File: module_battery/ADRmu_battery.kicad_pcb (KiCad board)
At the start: 2 copper layers, 160 x 100 mm, 1 part, among them J101 Harting 09042326831

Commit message: asdf
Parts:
- removed J101: Harting 09042326831, Connector_DIN:DIN41612_D_2x16_Male_Horizontal_THT
- added B101: BK-18650-PC8, ADRmu_battery_Library:BK-18650-PC8, F.Cu at (115.0, 70.0)
- added J1: Harting 09042326831, Connector_DIN:DIN41612_D_2x16_Male_Horizontal_THT, F.Cu at (224.7, 60.6)

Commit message: asdf
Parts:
- added C101: 1u 50V, Capacitor_SMD:C_0805_2012Metric, F.Cu at (148.6, 97.8)
- added C102: 1u 50V, Capacitor_SMD:C_0805_2012Metric, F.Cu at (144.1, 94.8)
- added C103: 1u 50V, Capacitor_SMD:C_0805_2012Metric, F.Cu at (144.1, 91.8)
- added C104: 1u 50V, Capacitor_SMD:C_0805_2012Metric, F.Cu at (139.8, 104.7)
- added C105: 1u 50V, Capacitor_SMD:C_0805_2012Metric, F.Cu at (153.0, 91.8)
- added C106: 1u 50V, Capacitor_SMD:C_0805_2012Metric, F.Cu at (148.6, 91.8)
- added C107: 1u 50V, Capacitor_SMD:C_0805_2012Metric, F.Cu at (135.4, 104.7)
- added C108: 100n 50V, Capacitor_SMD:C_0805_2012Metric, F.Cu at (144.1, 97.8)
- added C109: 100n 50V, Capacitor_SMD:C_0805_2012Metric, F.Cu at (148.6, 94.8)
- added C110: 100n 50V, Capacitor_SMD:C_0805_2012Metric, F.Cu at (142.9, 101.1)
- added C111: 100n 50V, Capacitor_SMD:C_0805_2012Metric, F.Cu at (168.9, 111.8)
- added D101: 1N4148, Diode_SMD:D_SOD-123, F.Cu at (169.6, 104.0)
- added D102: 16V, Diode_SMD:D_SOT-23_ANK, F.Cu at (168.9, 108.0)
- added NT101: NetTie_2, NetTie:NetTie-2_SMD_Pad2.0mm, F.Cu at (136.9, 101.4)
- added Q101: Q_NMOS_GDS, Package_TO_SOT_SMD:TO-252-2, F.Cu at (160.6, 114.4)
- added Q102: Q_NMOS_GDS, Package_TO_SOT_SMD:TO-252-2, F.Cu at (160.6, 106.4)
- added R101: 1k, Resistor_SMD:R_0805_2012Metric, F.Cu at (153.0, 97.7)
- added R102: 47, Resistor_SMD:R_0805_2012Metric, F.Cu at (157.4, 97.6)
- added R103: 47, Resistor_SMD:R_0805_2012Metric, F.Cu at (157.5, 94.7)
- added R104: 47, Resistor_SMD:R_0805_2012Metric, F.Cu at (157.5, 91.7)
- added R105: 47, Resistor_SMD:R_0805_2012Metric, F.Cu at (144.3, 104.1)
- added R106: 47, Resistor_SMD:R_0805_2012Metric, F.Cu at (147.4, 100.8)
- added R107: 100, Resistor_SMD:R_0805_2012Metric, F.Cu at (151.8, 100.8)
- added R108: 1, Resistor_SMD:R_0805_2012Metric, F.Cu at (148.7, 103.7)
- added R109: 100, Resistor_SMD:R_0805_2012Metric, F.Cu at (153.0, 94.8)
- added R110: 5k1, Resistor_SMD:R_0805_2012Metric, F.Cu at (168.9, 114.7)
- added R111: 10M, Resistor_SMD:R_0805_2012Metric, F.Cu at (174.6, 103.8)
- added R112: 5k1, Resistor_SMD:R_0805_2012Metric, F.Cu at (177.8, 106.8)
- added R113: 3M, Resistor_SMD:R_0805_2012Metric, F.Cu at (173.3, 110.1)
- added R114: 470k, Resistor_SMD:R_0805_2012Metric, F.Cu at (173.3, 107.2)
- added R115: 1M, Resistor_SMD:R_0805_2012Metric, F.Cu at (179.1, 103.8)
- added R116: 10k, Resistor_SMD:R_0805_2012Metric, F.Cu at (175.3, 94.0)
- added R117: 200k, Resistor_SMD:R_0805_2012Metric, F.Cu at (166.4, 94.0)
- added R118: 10k, Resistor_SMD:R_0805_2012Metric, F.Cu at (166.4, 96.9)
- added R119: 10k, Resistor_SMD:R_0805_2012Metric, F.Cu at (170.8, 96.9)
- added TH101: Thermistor_NTC, Resistor_SMD:R_0805_2012Metric, F.Cu at (170.8, 94.0)
- added U101: BQ77915, Package_SO:TSSOP-24_4.4x7.8mm_P0.65mm, F.Cu at (137.5, 94.9)
- moved B101 64.3 mm to (178.9, 63.5), turned to -90 degrees
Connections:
- B101 pad 1: unconnected-(B101-Pad1) -> +BATT
- B101 pad 8: unconnected-(B101-Pad8) -> -BATT

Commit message: asdf
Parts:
- added C112: 100n 50V, Capacitor_SMD:C_0805_2012Metric, B.Cu at (215.9, 111.8)
- added D103: LT Y8SG-V2AB-36, LED_SMD:LED_1206_3216Metric, F.Cu at (77.5, 76.2)
- added D104: LT Y8SG-V2AB-36, LED_SMD:LED_1206_3216Metric, F.Cu at (74.9, 68.6)
- added R120: 10k, Resistor_SMD:R_0805_2012Metric, B.Cu at (75.3, 73.7)
- added R121: 1R4 2W, Resistor_SMD:R_2512_6332Metric, B.Cu at (205.7, 82.5)
- added R122: 10k, Resistor_SMD:R_0805_2012Metric, B.Cu at (74.9, 64.8)
- added U102: LM317_TO-263, Package_TO_SOT_SMD:TO-263-2, B.Cu at (205.7, 108.0)
- C101, C102, C103, C104, C105, C106, C109, C110, C111, D101, D102, NT101, Q101, Q102, R101, R107, R109, R110, R111, R113, R116, R117, R119, TH101: moved to B.Cu
- C107: renamed from C108; moved to B.Cu
- C108: renamed from C107; moved to B.Cu
- R102, R103, R104, R105, R106: value 47 -> 164; moved to B.Cu
- R108: value 1 -> 60mR; moved to B.Cu
- R112: renamed from R115; moved to B.Cu
- R114: renamed from R112; moved to B.Cu
- R115: renamed from R118; moved to B.Cu
- R118: renamed from R114; moved to B.Cu
- U101: value BQ77915 -> BQ7791500; moved to B.Cu
- moved R112 216.6 mm to (-37.0, 119.3), turned to 180 degrees
- moved R114 214.0 mm to (-35.7, 122.2), turned to 180 degrees
- moved R116 209.1 mm to (-33.2, 109.4), turned to 180 degrees
- moved R111 207.8 mm to (-32.6, 119.3), turned to 180 degrees
- moved R113 205.2 mm to (-31.3, 125.6), turned to 180 degrees
- moved R118 205.2 mm to (-31.3, 122.6), turned to 180 degrees
- moved R119 200.3 mm to (-28.8, 112.4), turned to 180 degrees
- moved TH101 200.3 mm to (-28.8, 109.4), turned to 180 degrees
- moved D101 197.7 mm to (-27.5, 119.5), turned to 180 degrees
- moved C111 196.4 mm to (-26.9, 127.2), turned to 180 degrees
- moved D102 196.4 mm to (-26.9, 123.4), turned to 180 degrees
- moved R110 196.4 mm to (-26.9, 130.2), turned to 180 degrees
- moved R117 191.5 mm to (-24.4, 109.4), turned to 180 degrees
- moved R115 191.5 mm to (-24.4, 112.4), turned to 180 degrees
- moved Q101 179.9 mm to (-18.6, 129.9), turned to 180 degrees
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- renumbered J1 to J101
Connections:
- net Net-(J1-Pada20) renamed /in+
- C111 pad 2: Net-(Q102-Pad3) -> /-out
- D102 pad 2: Net-(Q102-Pad3) -> /-out
- J101 pad a10: Net-(J1-Pada10) -> unconnected-(J101-Pada10)
- J101 pad a12: Net-(J1-Padc16) -> unconnected-(J101-Pada12)
- J101 pad a14: Net-(J1-Pada14) -> unconnected-(J101-Pada14)
- J101 pad a16: Net-(J1-Padc16) -> unconnected-(J101-Pada16)
- J101 pad a18: Net-(J1-Pada18) -> unconnected-(J101-Pada18)
- J101 pad a2: Net-(J1-Pada2) -> +BATT
- J101 pad a22: Net-(J1-Padc16) -> GND
- J101 pad a24: Net-(J1-Padc16) -> GND
- J101 pad a26: Net-(J1-Pada26) -> unconnected-(J101-Pada26)
- J101 pad a28: Net-(J1-Pada28) -> unconnected-(J101-Pada28)
- J101 pad a30: Net-(J1-Pada30) -> unconnected-(J101-Pada30)
- J101 pad a32: Net-(J1-Pada32) -> unconnected-(J101-Pada32)
- J101 pad a4: Net-(J1-Padc16) -> /-out
- J101 pad a6: Net-(J1-Pada6) -> unconnected-(J101-Pada6)
- J101 pad a8: Net-(J1-Padc16) -> unconnected-(J101-Pada8)
- J101 pad c10: Net-(J1-Pada10) -> unconnected-(J101-Padc10)
- J101 pad c12: Net-(J1-Padc16) -> unconnected-(J101-Padc12)
- J101 pad c14: Net-(J1-Pada14) -> unconnected-(J101-Padc14)
- J101 pad c16: Net-(J1-Padc16) -> unconnected-(J101-Padc16)
- J101 pad c18: Net-(J1-Pada18) -> unconnected-(J101-Padc18)
- J101 pad c2: Net-(J1-Pada2) -> +BATT
- J101 pad c22: Net-(J1-Padc16) -> GND
- J101 pad c24: Net-(J1-Padc16) -> GND
- J101 pad c26: Net-(J1-Pada26) -> unconnected-(J101-Padc26)
- J101 pad c28: Net-(J1-Pada28) -> unconnected-(J101-Padc28)
- J101 pad c30: Net-(J1-Pada30) -> unconnected-(J101-Padc30)
- J101 pad c32: Net-(J1-Pada32) -> unconnected-(J101-Padc32)
- J101 pad c4: Net-(J1-Padc16) -> /-out
- J101 pad c6: Net-(J1-Pada6) -> unconnected-(J101-Padc6)
- J101 pad c8: Net-(J1-Padc16) -> unconnected-(J101-Padc8)
- Q102 pad 3: Net-(Q102-Pad3) -> /-out
- R113 pad 1: Net-(Q102-Pad3) -> /-out
- R118 pad 1: Net-(Q102-Pad3) -> /-out
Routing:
- net Net-(B101-Pad4): track 0.00 -> 99.2 mm
- net Net-(B101-Pad6): track 0.00 -> 88.6 mm
- net Net-(B101-Pad2): track 0.00 -> 88.4 mm
- net /in+: track 0.00 -> 16.9 mm
- net GND: track 0.00 -> 14.3 mm
- net +BATT: track 0.00 -> 0.54 mm
- added copper zone on B.Cu, net +BATT
- added copper zone on F.Cu, net +BATT
- added copper zone on B.Cu, net GND
- added copper zone on F.Cu, net GND
- added copper zone on B.Cu, net Net-(R121-Pad1)
- added copper zone on F.Cu, net Net-(R121-Pad1)

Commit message: asdf
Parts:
- C101, C102, C103, C104, C105, C106, C107, C108, C109, C110, C111, C112, D101, D102, NT101, Q101, Q102, R101, R102, R103, R104, R105, R106, R107, R108, R109, R110, R111, R112, R113, R114, R115, R116, R117, R118, R119, R120, R121, R122, U101, U102: moved to F.Cu
- moved TH101 156.5 mm to (127.0, 94.5), turned to 90 degrees
- moved R122 152.5 mm to (216.5, 121.5), turned to -90 degrees
- moved R116 141.6 mm to (107.5, 93.8), turned to 0 degrees
- moved R119 137.0 mm to (107.4, 98.4)
- moved R118 134.5 mm to (101.5, 101.5), turned to 90 degrees
- moved R115 133.6 mm to (107.5, 91.6), turned to 0 degrees
- moved R117 132.6 mm to (107.5, 96.4)
- moved R112 132.5 mm to (95.3, 113.9)
- moved R114 131.5 mm to (95.3, 111.4)
- moved R111 125.7 mm to (92.3, 105.3), turned to -90 degrees
- moved R110 124.5 mm to (95.3, 106.3), turned to 0 degrees
- moved R113 124.3 mm to (92.3, 112.9), turned to -90 degrees
- moved D101 121.9 mm to (94.3, 116.5), turned to 0 degrees
- moved C111 120.6 mm to (92.3, 109.1), turned to -90 degrees
- moved D102 116.7 mm to (89.8, 119.0), turned to 0 degrees
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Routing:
- net /-out: track 0.00 -> 250.7 mm, vias 0 -> 2
- net Net-(D104-Pad2): track 0.00 -> 232.8 mm, vias 0 -> 2
- net +BATT: track 0.54 -> 99.6 mm
- net -BATT: track 0.00 -> 84.2 mm
- net Net-(B101-Pad2): track 88.4 -> 166.2 mm
- net Net-(B101-Pad4): track 99.2 -> 153.0 mm
- net Net-(B101-Pad6): track 88.6 -> 139.8 mm
- net Net-(D103-Pad2): track 0.00 -> 38.5 mm, vias 0 -> 2
- net Net-(R116-Pad1): track 0.00 -> 25.3 mm, vias 0 -> 1
- net /in+: track 16.9 -> 37.8 mm
- net Net-(C101-Pad2): track 0.00 -> 20.8 mm
- net Net-(C102-Pad2): track 0.00 -> 19.6 mm
- net Net-(C111-Pad1): track 0.00 -> 19.1 mm
- net Net-(C103-Pad2): track 0.00 -> 17.9 mm
- net Net-(C106-Pad1): track 0.00 -> 17.0 mm
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
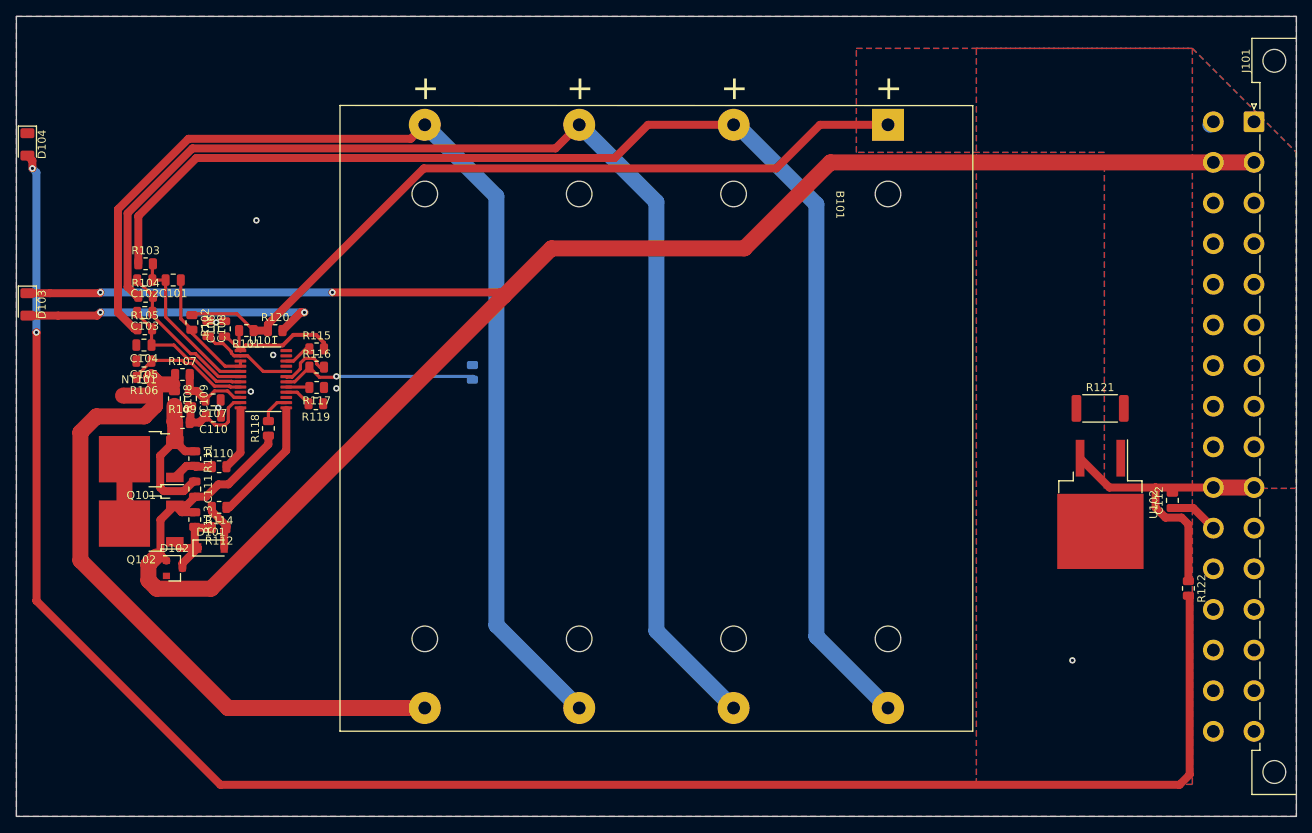
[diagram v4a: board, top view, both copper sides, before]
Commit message: Battery charger Rev 0.1 finished
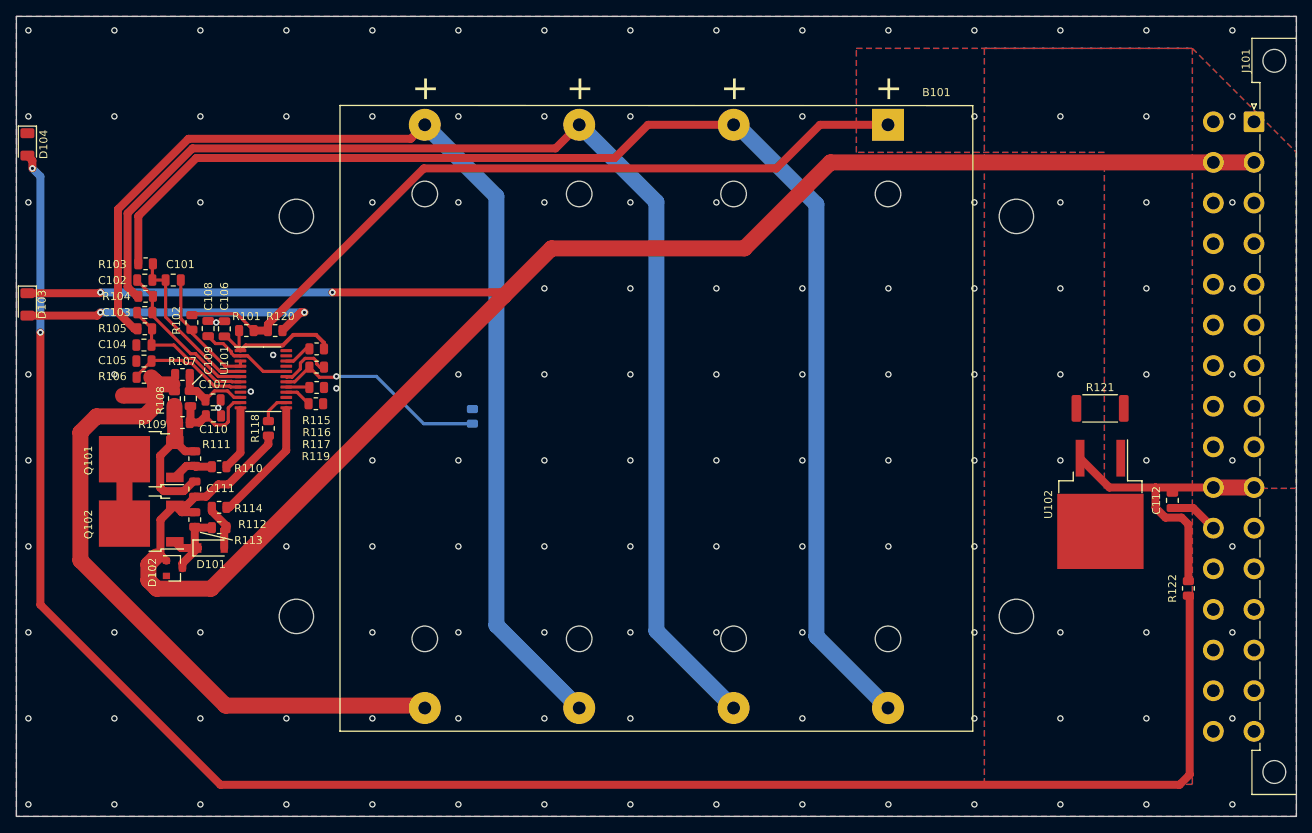
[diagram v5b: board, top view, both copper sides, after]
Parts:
- added H101: MountingHole, MountingHole:MountingHole_4.3mm_M4, F.Cu at (105.0, 75.0)
- added H102: MountingHole, MountingHole:MountingHole_4.3mm_M4, F.Cu at (195.0, 125.0)
- added H103: MountingHole, MountingHole:MountingHole_4.3mm_M4, F.Cu at (195.0, 75.0)
- added H104: MountingHole, MountingHole:MountingHole_4.3mm_M4, F.Cu at (105.0, 125.0)
- moved TH101 5.50 mm to (127.0, 100.0)
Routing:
- net Net-(R116-Pad1): track 25.3 -> 27.1 mm
- net -BATT: track 84.2 -> 83.1 mm
- net +BATT: track 99.6 -> 98.8 mm, vias 0 -> 12
- net Net-(C102-Pad2): track 19.6 -> 18.9 mm
- net Net-(R121-Pad1): vias 1 -> 8
- net GND: vias 6 -> 109

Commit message: Battery module Rev 0.2
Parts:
- removed the R121 at (205.5, 99.0)
- added R116: 9.1M, Resistor_SMD:R_0805_2012Metric, F.Cu at (192.0, 66.0)
- added R117: 680k, Resistor_SMD:R_0805_2012Metric, F.Cu at (202.0, 108.5)
- added R123: 10k, Resistor_SMD:R_0805_2012Metric, F.Cu at (210.0, 105.0)
- added R124: 1k2, Resistor_SMD:R_0805_2012Metric, F.Cu at (210.0, 108.6)
- added TH102: CMFB3435103FNT, Resistor_SMD:R_0805_2012Metric, B.Cu at (174.0, 100.0)
- R122: renamed from R120; value 10k -> 49k9
- R125: renamed from R122; value 10k -> 49k9
- TH101: value Thermistor_NTC -> CMFB3435103FNT
- U102: value LM317_TO-263 -> LTC4079; footprint Package_TO_SOT_SMD:TO-263-2 -> Package_DFN_QFN:DFN-10-1EP_3x3mm_P0.5mm_EP1.65x2.38mm
- moved R125 6.58 mm to (215.5, 115.0)
- moved C112 4.88 mm to (210.0, 112.4), turned to -90 degrees
- moved U102 1.12 mm to (206.0, 112.0), turned to 180 degrees
- turned TH101 to -90 degrees
- renumbered H102 to H101, H101 to H102, H104 to H103, H103 to H104, R116 to R118, R117 to R119, R118 to R120, R119 to R121
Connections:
- C111 pad 2: /-out -> /-i/o
- C112 pad 1: GND -> /-i/o
- D102 pad 2: /-out -> /-i/o
- D103 pad 1: /-out -> /-i/o
- D104 pad 1: GND -> Net-(D104-Pad1)
- J101 pad a22: GND -> /-i/o
- J101 pad a24: GND -> /-i/o
- J101 pad a4: /-out -> /-i/o
- J101 pad c22: GND -> /-i/o
- J101 pad c24: GND -> /-i/o
- J101 pad c4: /-out -> /-i/o
- Q102 pad 3: /-out -> /-i/o
- R113 pad 1: /-out -> /-i/o
- R120 pad 1: /-out -> /-i/o
- U102 pad 1: +BATT -> /in+
- U102 pad 2: Net-(R121-Pad1) -> /in+
- U102 pad 3: /in+ -> Net-(R124-Pad2)
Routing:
- net /-out: track 250.7 -> 0.00 mm, vias 2 -> 0
- net Net-(D104-Pad1): track 0.00 -> 206.3 mm, vias 0 -> 2
- net +BATT: track 98.8 -> 209.4 mm, vias 12 -> 0
- net Net-(R116-Pad1): track 0.00 -> 52.0 mm
- net Net-(R123-Pad1): track 0.00 -> 46.2 mm, vias 0 -> 1
- net /-i/o: track 0.00 -> 44.6 mm, vias 0 -> 119
- net /in+: track 37.8 -> 19.0 mm
- net GND: track 6.16 -> 18.8 mm, vias 109 -> 6
- net Net-(R123-Pad2): track 0.00 -> 6.94 mm
- net Net-(R117-Pad1): track 0.00 -> 5.99 mm
- net Net-(R124-Pad2): track 0.00 -> 4.17 mm
- net Net-(C101-Pad1): track 15.6 -> 17.4 mm
- net Net-(R118-Pad1): track 27.1 -> 26.3 mm
- net Net-(D104-Pad2): track 232.8 -> 232.1 mm
- net Net-(R121-Pad1): vias 8 -> 0
- added copper zone on B.Cu, net /-i/o
- added copper zone on F.Cu, net /-i/o
- removed copper zone on B.Cu, net +BATT
- removed copper zone on F.Cu, net +BATT
- removed copper zone on B.Cu, net Net-(R121-Pad1)
- removed copper zone on F.Cu, net Net-(R121-Pad1)
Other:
- board text added: "ADRmu Battery module Rev 0.2"

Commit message: asdf
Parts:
- added C112: 100n 50V, Capacitor_SMD:C_0805_2012Metric, F.Cu at (213.9, 68.0)
- added C113: 220u 16V, Capacitor_THT:CP_Radial_D10.0mm_P5.00mm, F.Cu at (212.0, 61.4)
- added C115: 220u 16V, Capacitor_THT:CP_Radial_D10.0mm_P5.00mm, F.Cu at (211.0, 118.6)
- added U103: L7812, Package_TO_SOT_SMD:TO-252-2, F.Cu at (205.0, 68.0)
- renumbered C112 to C114, R118 to R116, R119 to R117, R120 to R118, R121 to R119, R122 to R120, R116 to R121, R117 to R122
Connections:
- J101 pad a2: +BATT -> Net-(C113-Pad1)
- J101 pad c2: +BATT -> Net-(C113-Pad1)
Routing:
- net /-i/o: track 44.6 -> 6.46 mm, vias 119 -> 118
- net Net-(C113-Pad1): track 0.00 -> 19.0 mm
- net Net-(D104-Pad1): track 206.3 -> 193.9 mm
- net /in+: track 19.0 -> 24.4 mm
- net +BATT: track 209.4 -> 205.4 mm

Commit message: asdf
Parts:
- removed NT101: NetTie_2, NetTie:NetTie-2_SMD_Pad2.0mm
- added C116: 1u 50V, Capacitor_SMD:C_0805_2012Metric, F.Cu at (246.7, 118.1)
- added D105: BZX84C10, Package_TO_SOT_SMD:SOT-23, F.Cu at (93.3, 144.8)
- added D106: LT Y8SG-V2AB-36, LED_SMD:LED_1206_3216Metric, F.Cu at (71.4, 136.0)
- added D107: 1N4148, Diode_SMD:D_SOD-123, F.Cu at (86.4, 140.1)
- added D108: 1N4148, Diode_SMD:D_SOD-123, F.Cu at (88.9, 140.1)
- added D109: LT Y8SG-V2AB-36, LED_SMD:LED_1206_3216Metric, F.Cu at (71.4, 126.0)
- added D110: 1N4148, Diode_SMD:D_SOD-123, F.Cu at (78.1, 140.8)
- added D111: 1N4148, Diode_SMD:D_SOD-123, F.Cu at (80.8, 140.8)
- added D112: LT Y8SG-V2AB-36, LED_SMD:LED_1206_3216Metric, F.Cu at (71.4, 116.0)
- added D113: 1N4148, Diode_SMD:D_SOD-123, F.Cu at (78.1, 131.8)
- added D114: 1N4148, Diode_SMD:D_SOD-123, F.Cu at (80.6, 131.8)
- added D115: LT Y8SG-V2AB-36, LED_SMD:LED_1206_3216Metric, F.Cu at (71.4, 106.0)
- added F101: 2A, Fuse:Fuse_1812_4532Metric, F.Cu at (104.5, 135.9)
- added Q103: MMBFJ111, Package_TO_SOT_SMD:SOT-23, F.Cu at (88.9, 144.5)
- added Q104: MMBFJ111, Package_TO_SOT_SMD:SOT-23, F.Cu at (88.9, 135.6)
- added Q105: MMBFJ111, Package_TO_SOT_SMD:SOT-23, F.Cu at (80.8, 136.4)
- added Q106: MMBFJ111, Package_TO_SOT_SMD:SOT-23, F.Cu at (80.6, 127.4)
- added R126: 5k1, Resistor_SMD:R_0805_2012Metric, F.Cu at (85.7, 144.5)
- added R127: 5k1, Resistor_SMD:R_0805_2012Metric, F.Cu at (85.8, 135.6)
- added R128: 5k1, Resistor_SMD:R_0805_2012Metric, F.Cu at (77.6, 136.4)
- added R129: 1k2, Resistor_SMD:R_0805_2012Metric, F.Cu at (77.2, 127.4)
- added R130: 5k1, Resistor_SMD:R_0805_2012Metric, F.Cu at (258.2, 120.7)
- added R131: 10k, Resistor_SMD:R_0805_2012Metric, F.Cu at (252.7, 118.1)
- added U104: LM317_TO-252, Package_TO_SOT_SMD:TO-252-2, F.Cu at (250.2, 125.7)
- C114: value 100n 50V -> 1u 50V
- C115: value 220u 16V -> 1u 50V; footprint Capacitor_THT:CP_Radial_D10.0mm_P5.00mm -> Capacitor_SMD:C_0805_2012Metric
- R102, R103, R104, R105, R106: value 164 -> 33
- moved C114 44.5 mm to (249.9, 132.1), turned to 180 degrees
- moved C115 36.7 mm to (245.1, 132.1), turned to 0 degrees
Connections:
- C114 pad 1: /-i/o -> Net-(U102-Pad1)
- C114 pad 2: /in+ -> /-i/o
- R106 pad 1: -BATT -> GND
- R107 pad 1: -BATT -> GND
- R108 pad 1: -BATT -> GND
- U102 pad 1: /in+ -> Net-(U102-Pad1)
- U102 pad 2: /in+ -> Net-(U102-Pad1)
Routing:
- net +BATT: track 205.4 -> 278.0 mm, vias 0 -> 2
- net -BATT: track 83.1 -> 14.6 mm
- net GND: track 18.8 -> 82.9 mm
- net Net-(D109-Pad2): track 0.00 -> 37.4 mm
- net Net-(D108-Pad1): track 0.00 -> 31.5 mm
- net Net-(D115-Pad2): track 0.00 -> 27.8 mm
- net Net-(D112-Pad2): track 0.00 -> 24.8 mm
- net Net-(D106-Pad2): track 0.00 -> 22.1 mm
- net Net-(D111-Pad1): track 0.00 -> 10.7 mm
- net Net-(D105-Pad1): track 0.00 -> 10.2 mm
- net Net-(D104-Pad2): track 232.1 -> 226.6 mm
- net Net-(D110-Pad1): track 0.00 -> 4.35 mm
- net Net-(D107-Pad1): track 0.00 -> 4.35 mm
- net Net-(D113-Pad1): track 0.00 -> 4.35 mm
- net Net-(Q106-Pad3): track 0.00 -> 2.92 mm
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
